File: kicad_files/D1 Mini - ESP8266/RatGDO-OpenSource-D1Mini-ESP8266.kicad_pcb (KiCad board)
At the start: 2 copper layers, 55 x 70 mm, 12 parts, among them J1 Screw_Terminal_01x03, J2 Screw_Terminal_01x03, Q1 2N7002, Q2 AO3400A, U1 WeMos_D1_mini

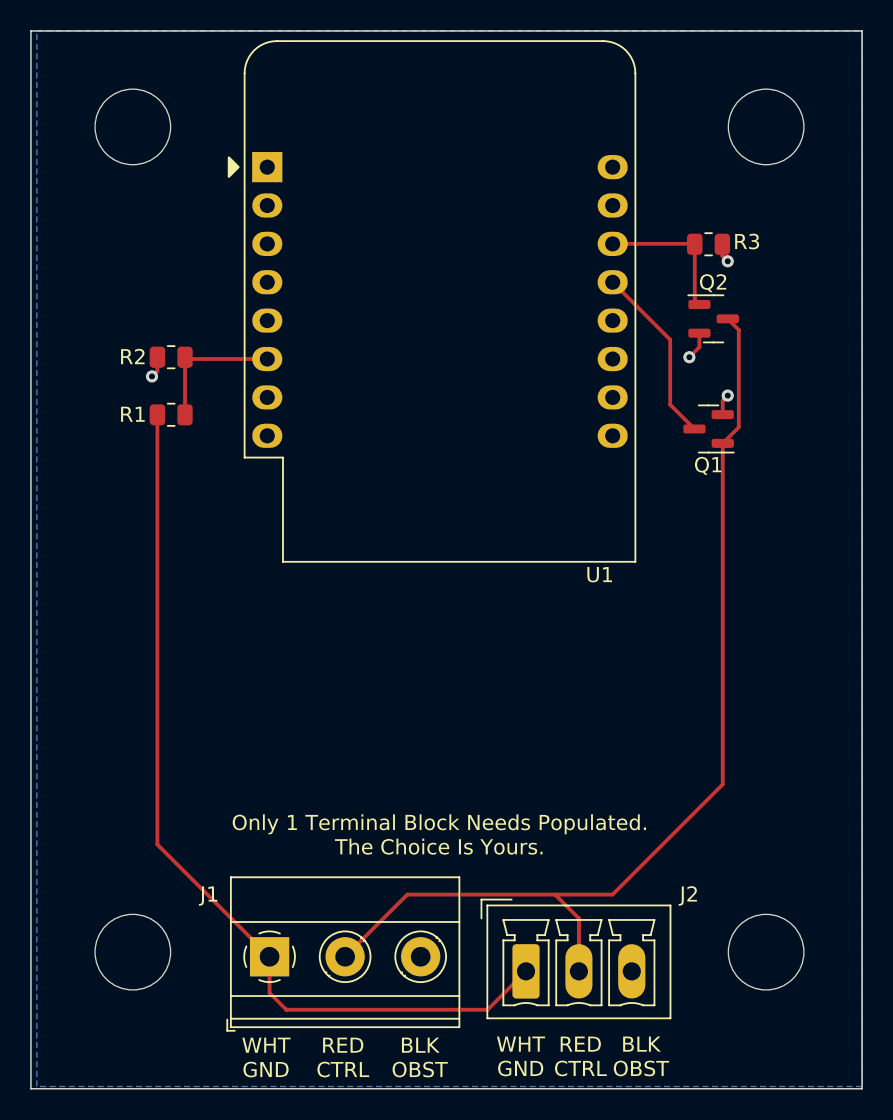
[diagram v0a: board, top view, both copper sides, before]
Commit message: Fixed Bad PCB Labeling
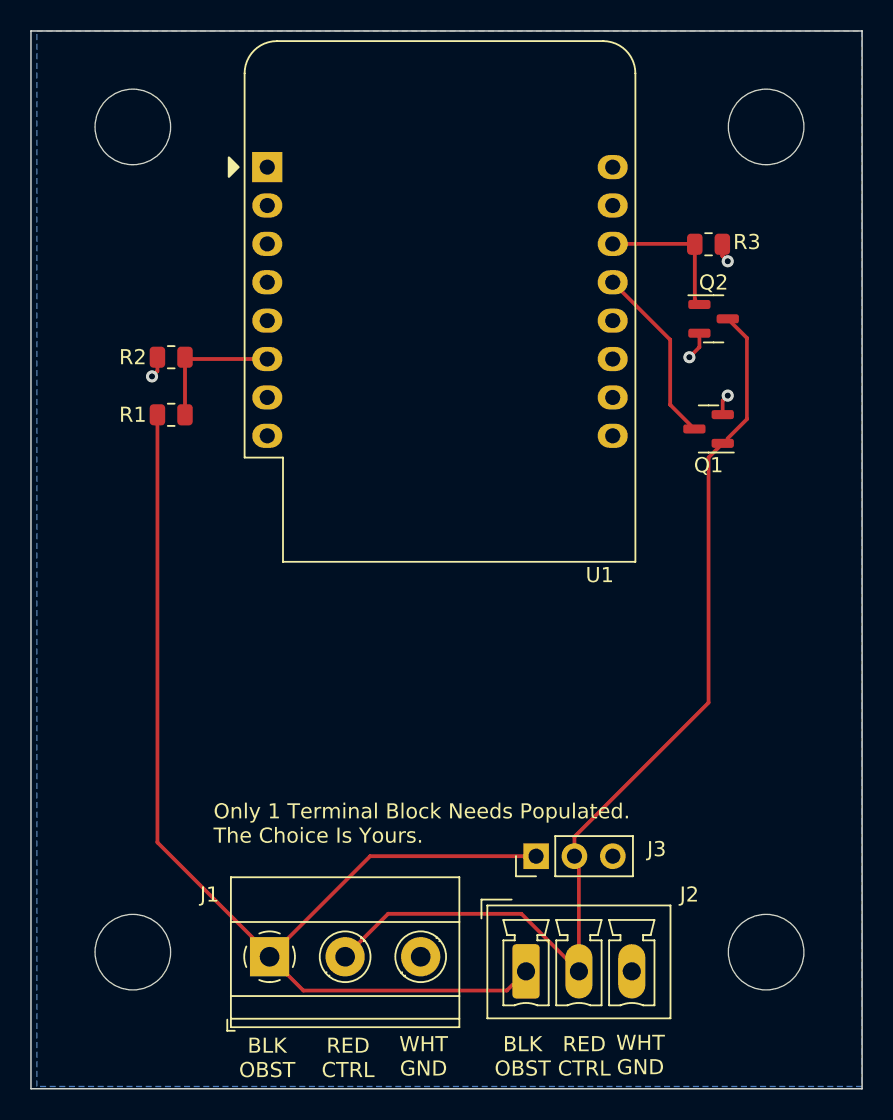
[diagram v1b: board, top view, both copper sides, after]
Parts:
- added J3: Screw_Terminal_01x03, Connector_PinHeader_2.54mm:PinHeader_1x03_P2.54mm_Vertical, F.Cu at (147.3, 111.8)
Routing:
- net Net-(J1-Blk/Obst): track 59.8 -> 77.8 mm
- net Net-(J1-Red/Cntrl): track 67.0 -> 66.3 mm

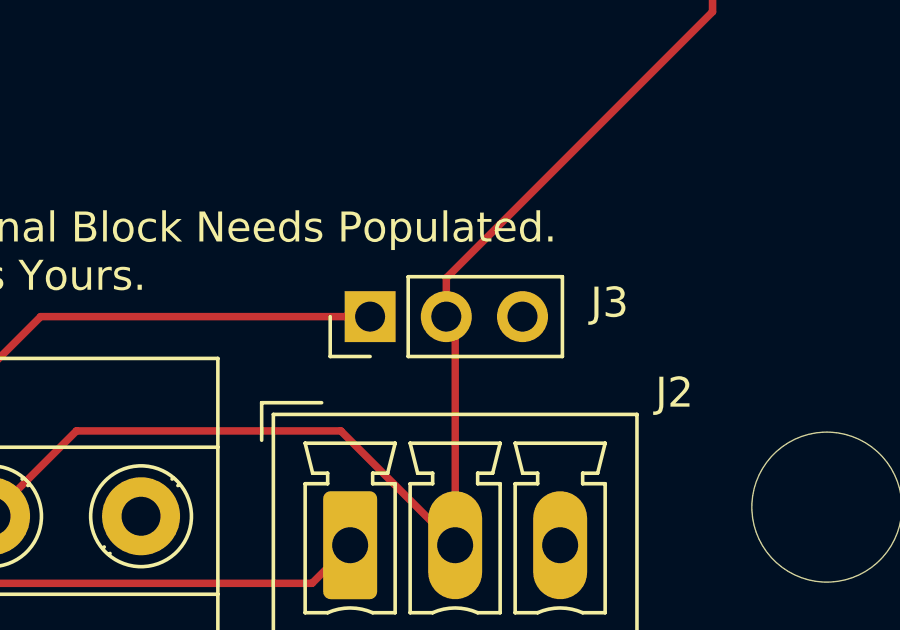
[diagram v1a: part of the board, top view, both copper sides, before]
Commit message: Change Pin Header to Pin Socket
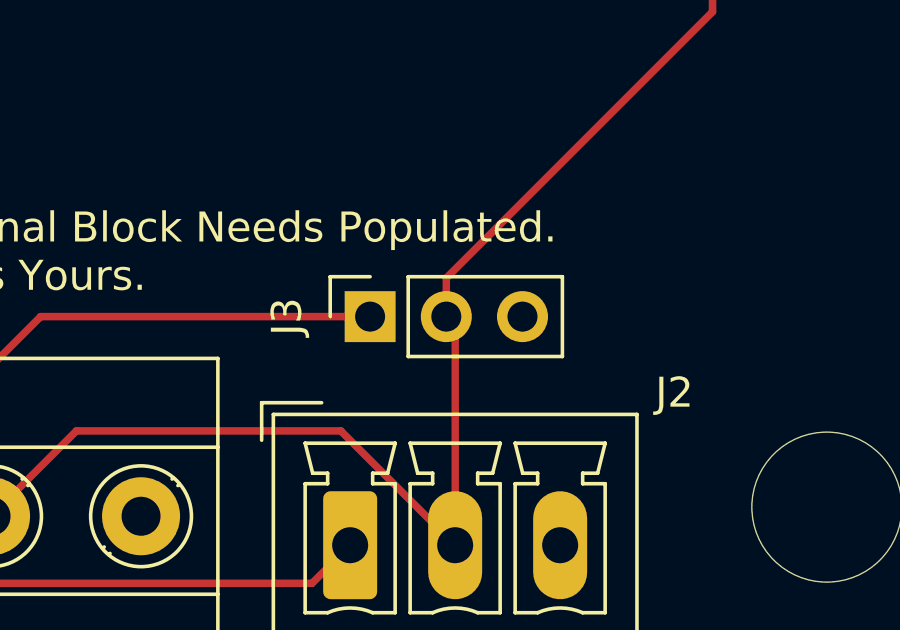
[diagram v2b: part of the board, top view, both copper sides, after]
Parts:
- J3: footprint Connector_PinHeader_2.54mm:PinHeader_1x03_P2.54mm_Vertical -> Connector_PinSocket_2.54mm:PinSocket_1x03_P2.54mm_Vertical
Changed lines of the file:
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@@
     (pad "" np_thru_hole circle (at 0 0) (size 5 5) (drill 5) (layers "F&B.Cu" "*.Mask"))
   )
-  (footprint "Connector_PinHeader_2.54mm:PinHeader_1x03_P2.54mm_Vertical" (layer "F.Cu")
+  (footprint "Connector_PinSocket_2.54mm:PinSocket_1x03_P2.54mm_Vertical" (layer "F.Cu")
     (at 147.335 111.76 90)
-    (descr "Through hole straight pin header, 1x03, 2.54mm pitch, single row")
-    (tags "Through hole pin header THT 1x03 2.54mm single row")
+    (descr "Through hole straight socket strip, 1x03, 2.54mm pitch, single row (from Kicad 4.0.7), script generated")
+    (tags "Through hole socket strip THT 1x03 2.54mm single row")
     (property "Sheetfile" "RatGDO-OpenSource-D1Mini-ESP8266.kicad_sch")
     (property "Sheetname" "")
@@
     (property "ki_keywords" "screw terminal")
     (attr through_hole)
-    (fp_text reference "J3" (at 0.46243 7.981344) (layer "F.SilkS")
+    (fp_text reference "J3" (at 0 -2.77 90) (layer "F.SilkS")
         (effects (font (size 1 1) (thickness 0.15)))
     )
-    (fp_text value "Screw_Terminal_01x03" (at 0 7.41 90) (layer "F.Fab")
+    (fp_text value "Screw_Terminal_01x03" (at 0 7.85 90) (layer "F.Fab")
         (effects (font (size 1 1) (thickness 0.15)))
     )
-    (fp_text user "${REFERENCE}" (at 0 2.54) (layer "F.Fab")
+    (fp_text user "${REFERENCE}" (at 0 2.54 180) (layer "F.Fab")
         (effects (font (size 1 1) (thickness 0.15)))
     )
-    (fp_line (start -1.33 -1.33) (end 0 -1.33)
-      (stroke (width 0.12) (type solid)) (layer "F.SilkS"))
-    (fp_line (start -1.33 0) (end -1.33 -1.33)
-      (stroke (width 0.12) (type solid)) (layer "F.SilkS"))
     (fp_line (start -1.33 1.27) (end -1.33 6.41)
       (stroke (width 0.12) (type solid)) (layer "F.SilkS"))
@@
     (fp_line (start -1.33 6.41) (end 1.33 6.41)
       (stroke (width 0.12) (type solid)) (layer "F.SilkS"))
+    (fp_line (start 0 -1.33) (end 1.33 -1.33)
+      (stroke (width 0.12) (type solid)) (layer "F.SilkS"))
+    (fp_line (start 1.33 -1.33) (end 1.33 0)
+      (stroke (width 0.12) (type solid)) (layer "F.SilkS"))
     (fp_line (start 1.33 1.27) (end 1.33 6.41)
       (stroke (width 0.12) (type solid)) (layer "F.SilkS"))
-    (fp_line (start -1.8 -1.8) (end -1.8 6.85)
+    (fp_line (start -1.8 -1.8) (end 1.75 -1.8)
       (stroke (width 0.05) (type solid)) (layer "F.CrtYd"))
-    (fp_line (start -1.8 6.85) (end 1.8 6.85)
+    (fp_line (start -1.8 6.85) (end -1.8 -1.8)
       (stroke (width 0.05) (type solid)) (layer "F.CrtYd"))
-    (fp_line (start 1.8 -1.8) (end -1.8 -1.8)
+    (fp_line (start 1.75 -1.8) (end 1.75 6.85)
       (stroke (width 0.05) (type solid)) (layer "F.CrtYd"))
-    (fp_line (start 1.8 6.85) (end 1.8 -1.8)
+    (fp_line (start 1.75 6.85) (end -1.8 6.85)
       (stroke (width 0.05) (type solid)) (layer "F.CrtYd"))
-    (fp_line (start -1.27 -0.635) (end -0.635 -1.27)
+    (fp_line (start -1.27 -1.27) (end 0.635 -1.27)
       (stroke (width 0.1) (type solid)) (layer "F.Fab"))
-    (fp_line (start -1.27 6.35) (end -1.27 -0.635)
+    (fp_line (start -1.27 6.35) (end -1.27 -1.27)
       (stroke (width 0.1) (type solid)) (layer "F.Fab"))
-    (fp_line (start -0.635 -1.27) (end 1.27 -1.27)
+    (fp_line (start 0.635 -1.27) (end 1.27 -0.635)
       (stroke (width 0.1) (type solid)) (layer "F.Fab"))
-    (fp_line (start 1.27 -1.27) (end 1.27 6.35)
+    (fp_line (start 1.27 -0.635) (end 1.27 6.35)
       (stroke (width 0.1) (type solid)) (layer "F.Fab"))
     (fp_line (start 1.27 6.35) (end -1.27 6.35)
@@
     (pad "3" thru_hole oval (at 0 5.08 90) (size 1.7 1.7) (drill 1) (layers "*.Cu" "*.Mask")
       (net 15 "GND") (pinfunction "Wht/Gnd") (pintype "passive"))
-    (model "${KICAD6_3DMODEL_DIR}/Connector_PinHeader_2.54mm.3dshapes/PinHeader_1x03_P2.54mm_Vertical.wrl"
+    (model "${KICAD6_3DMODEL_DIR}/Connector_PinSocket_2.54mm.3dshapes/PinSocket_1x03_P2.54mm_Vertical.wrl"
       (offset (xyz 0 0 0))
       (scale (xyz 1 1 1))
